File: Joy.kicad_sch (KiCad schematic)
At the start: 22 parts, among them IC1 MC14512BDR2G, IC2 MC14512BDR2G, J1 DB9_Male, J2 DB9_Male, J3 DB25_Male

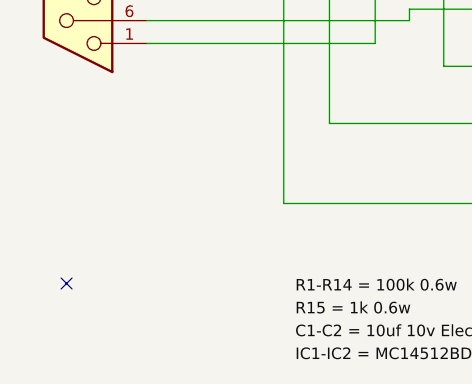
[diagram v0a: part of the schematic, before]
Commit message: Capacitors now through-hole, resistors 0805, cheaper connectors
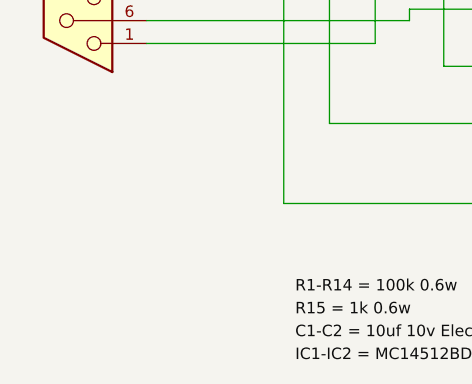
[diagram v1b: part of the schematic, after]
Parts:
- C1, C2: value (none) -> C_Polarized, 10uf Eletrolitic; footprint (none) -> Capacitor_THT:CP_Radial_D5.0mm_P2.00mm
- IC1, IC2: footprint MC14512BDR2G:MC14512BDR2G -> Package_SO:SOIC-16_3.9x9.9mm_P1.27mm
- J1, J2: footprint 5747840-6:5747840-6 -> MyFootprints:5747840-4
- J3: footprint 5747238-4:5747238-4 -> MyFootprints:5788794-1
- R1, R10, R11, R12, R13, R14, R15, R2, R3, R4, R5, R6, R7, R8, R9: footprint Resistor_SMD:R_1206_3216Metric_Pad1.30x1.75mm_HandSolder -> Resistor_SMD:R_0805_2012Metric_Pad1.20x1.40mm_HandSolder
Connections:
- no-connect marks 16 -> 15

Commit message: Updated module
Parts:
- C1, C2: value C_Polarized, 10uf Eletrolitic -> 10uF 10V
- R1, R10, R11, R12, R13, R14, R8, R9: value 100k -> 100K
- R15: value 1k -> 2K2
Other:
- note added: "+5V on Arc, 0V on Atari"
- note added: "Down"
- note added: "Fire-1"
- note added: "Fire-2 on Arc"
- note added: "Fire-3 on Arc, +5V on Atari"
- note added: "Left"
- note added: "Right"
- note added: "Up"
- moved on the sheet: C1, C2
